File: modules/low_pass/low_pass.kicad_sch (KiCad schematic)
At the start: 35 parts, among them U1 MCP6002-xSN, U2 VTL5C, U3 MCP6002-xSN, U4 MCP6002-xSN, U5 VTL5C, U6 VTL5C

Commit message: Introduced new low_pass gate.
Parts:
- removed C5, C6: 1nf, Capacitor_SMD:C_0402_1005Metric, symbol Device:C
- removed C7: 0.1uf, Capacitor_SMD:C_0402_1005Metric, symbol Device:C
- removed D1: LED, LED_SMD:LED_0603_1608Metric, symbol Device:LED
- removed R1, R2: 100k, Resistor_SMD:R_0402_1005Metric, symbol Device:R
- removed U1, U3, U4: MCP6002-xSN, Package_SO:SOIC-8-1EP_3.9x4.9mm_P1.27mm_EP2.29x3mm, symbol Amplifier_Operational:MCP6002-xSN
- removed U2, U5, U6: VTL5C, BreadModular_MISC:VTL5C, symbol Isolator:VTL5C
- removed V3: VSIN, symbol Simulation_SPICE:VSIN
- removed V4: 0, symbol Simulation_SPICE:VDC
- added R12, R13: 10k, symbol Device:R
- added R5: 1k, symbol Device:R
- added R6: 200k, symbol Device:R
- added U1, U3, U4: VTL5C, OptoDevice:PerkinElmer_VTL5C, symbol Isolator:VTL5C
- added U2, U5: MCP6002-xSN, symbol Amplifier_Operational:MCP6002-xSN
- added V3: 3.3, symbol Simulation_SPICE:VDC
- added V4: VSIN, symbol Simulation_SPICE:VSIN
- C1: footprint Capacitor_SMD:C_0402_1005Metric -> (none)
- C2, C3: value 0.1uf -> 10nf; footprint Capacitor_SMD:C_0402_1005Metric -> (none)
- C4: value 1nf -> 0.1uf; footprint Capacitor_SMD:C_0402_1005Metric -> (none)
- GND1: footprint Connector_PinHeader_2.54mm:PinHeader_1x05_P2.54mm_Vertical -> BreadModular_MISC:Power_Connector
- R1: renamed from R5; footprint Resistor_SMD:R_0402_1005Metric -> (none)
- R10: value 100k -> 10k; footprint Resistor_SMD:R_0402_1005Metric -> (none)
- R11: value 330 -> 1M; footprint Resistor_SMD:R_0805_2012Metric -> (none)
- R2: renamed from R6; footprint Resistor_SMD:R_0402_1005Metric -> (none)
- R3: value 100k -> 560; footprint Resistor_SMD:R_0402_1005Metric -> (none)
- R4: footprint Resistor_SMD:R_0402_1005Metric -> (none)
- R7: value 100k -> 200k; footprint Resistor_SMD:R_0402_1005Metric -> (none)
- R8: value 330 -> 560; footprint Resistor_SMD:R_0805_2012Metric -> (none)
- R9: value 1k -> 1M; footprint Resistor_SMD:R_0402_1005Metric -> (none)
- RV1: footprint BreadModular_Pots:Potentiometer_RV09 -> (none); Comment CV GAIN -> CUT OFF
- RV2: footprint BreadModular_Pots:Potentiometer_RV09 -> (none); Comment CUTOFF_FREQ -> CUT_OFF_CURVE
- V1: value 5 -> 3.3
- V_SUPPLY1: renamed from 5V1; footprint Connector_PinHeader_2.54mm:PinHeader_1x05_P2.54mm_Vertical -> BreadModular_MISC:Power_Connector
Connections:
- net AUDIO_IN: now also U1.4; no longer INPUT1.1 (Pin_1)
- net AUDIO_OUT: now also R5.2; no longer R9.2
- net GND: now also C4.2, INPUT1.5 (Pin_5), R11.1, R9.1, RV2.2, U1.1 (-), U2.4 (V-), U3.1 (-), U5.4 (V-), V3.2, V4.2; no longer C2.2, C3.2, R11.2
- net at R4.2: now also R3.2, RV1.2, U4.4
- net at R3.1: now also U1.2 (+), U3.2 (+)
- net at R4.1: now also R6.2
- net at RV2.1: now also R8.1
- net at RV2.3: no longer R8.1
- net at R7.1: now also RV1.3, U4.3, U5.6 (-), U5.7
- net V_SUPPLY: now reaches C4.1
- net V_SUPPLY: now also C1.1, R1.1, V1.1, V_SUPPLY1.1 (Pin_1), V_SUPPLY1.2 (Pin_2), V_SUPPLY1.3 (Pin_3), V_SUPPLY1.4 (Pin_4), V_SUPPLY1.5 (Pin_5), R12.1, U2.8 (V+), U5.8 (V+)
- net at R10.2: now also V3.1
- net at R7.2: now also R6.1
- net at R8.2: now also U4.1 (-)
- net at INPUT1.4 (Pin_4): now also R13.2
- net +2.5V renamed V_MID
- net V_MID: now also C2.2, C3.2, R13.1
- removed net +5V: C1.1, C2.1, C3.1, R1.1, V1.1, V_SUPPLY1.1 (Pin_1), V_SUPPLY1.2 (Pin_2), V_SUPPLY1.3 (Pin_3), V_SUPPLY1.4 (Pin_4), V_SUPPLY1.5 (Pin_5)
- net CUTOFF_CV_IN: no longer names the net of INPUT1.3 (Pin_3)
- net CUTOFF_CV_IN: now also R12.2
- net MOD_CV_IN renamed CUT_OFF_CV
- net CUT_OFF_CV: now also R10.1, R9.2, U5.3 (+); no longer RV1.2
- removed net PROCESSED_MOD_CV: R10.1, R3.2, RV2.2
- new net: C2.1, U1.3, U2.3 (+)
- new net: U4.2 (+), U5.1, U5.2 (-)
- new net: C3.1, U2.5 (+), U3.3
- new net: U2.1, U2.2 (-), U3.4
- new net: R5.1, U2.6 (-), U2.7
- new net GATE_CV: INPUT1.1 (Pin_1), R11.2, U5.5 (+), V4.1
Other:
- note added: "## 1. Core Filter This is a 2nd stage RC low pass filter with Vactrols controlling the resistors."
- note added: "## 2. Gate CV This is the CV that drives filter resistors. Since those are Vactrols, 0-VMax CV both does filter cut off modulation and act as a VCA. Here RV1, put a cap to where vactrol can drive. So, technically it's the cutt-off point controlled by a pot. pos=0.0 => low frequency pos=1.0 => high frequency"
- note added: "## 3. Cut Off CV This is another set of CV modulation, but it's changing the Cut Off position. (Just like rotating the RV1) Now RV2 act as changing the curve of CV. * pos=0.0 => Exponential Curve * pos=1.0 => Linear Curve"
- note removed: "## 1. PROCESS MOD CV Here we get some CV for modulation of the cuff of frquency. We assume it will be centered around 2.5V. Basically, this is summing amp with 2.5 as the virtual GND. It will wiggle around 2.5V. If no CV input, output is 2.5V."
- note removed: "## 2. Sallen Key Filter This is a very basic Sallen Key Filter and R1 and R2 is replaced with VTL5Cs."
- note removed: "## 3. Cut Of freqeuncy CutOff frequency of Sallen Key Filter is depend on the R1 and R2. They need to be equal too. Here we set R1 based on VTL5C. So it behaves based on the Voltage input for the LED. We set 2.5V as the base potentiometer is used to change the frequency. pos=0.0 is the minimum frequency. pos=1.0 is maximum freq."
- note removed: "## 4 CutOFF freq CV This is about adding a parallel resistor to the potentiometer resistance. So, we can set the maximum it can have. (Basically overriding the pot value) Yes, we use VTL5C. So: CV=0v => Maxiumum Resistance (So, 1M pot has full control) CV=5v => Min Resistance (Pot has no control and we are in the upper cutoff freq.)"
- note removed: "## 5. Driving LED for Modulation CV It's quite useful to see this. We can directly connect the LED to the processed CV out. But it leaks audio to the ground when a square wave is provided. So, we need to smooth out the input before sending to the LED. So, we use a RC filter and a opamp. We can use a transistor instead, but it tend to leak a bit. That's why we use am opamp."
- moved on the sheet: GND1, INPUT1, OUTPUT1, R1, R2, V1, V_SUPPLY1

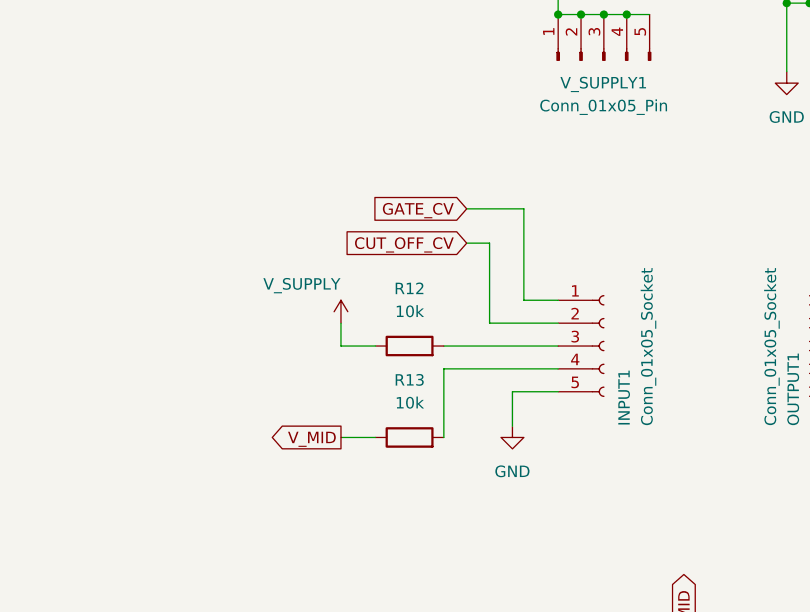
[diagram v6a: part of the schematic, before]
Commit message: Finalized the schematic of low_pass
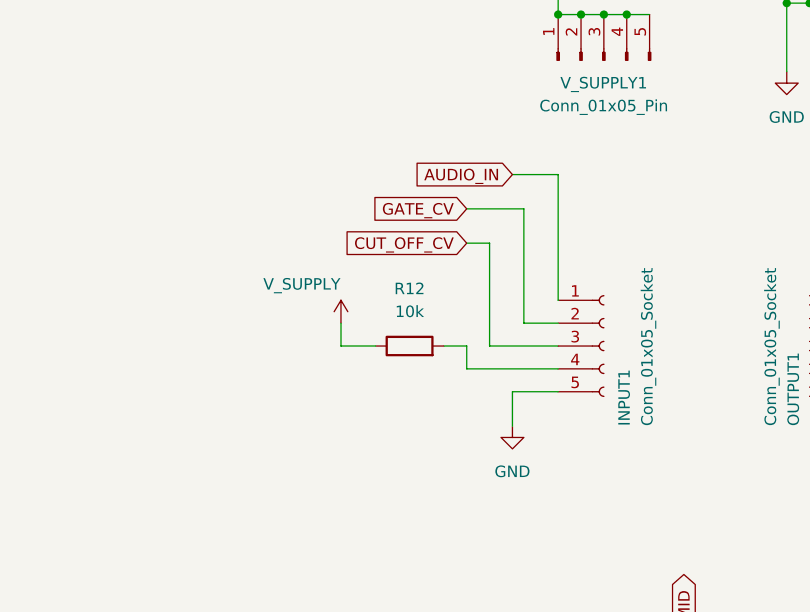
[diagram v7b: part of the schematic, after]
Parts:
- removed R13: 10k, symbol Device:R
- C1, C2, C3, C4: footprint (none) -> Capacitor_SMD:C_0402_1005Metric
- R1, R10, R11, R12, R2, R3, R4, R5, R6, R7, R8, R9: footprint (none) -> Resistor_SMD:R_0402_1005Metric
- RV1, RV2: footprint (none) -> BreadModular_Pots:Potentiometer_RV09
- U1, U3, U4: footprint OptoDevice:PerkinElmer_VTL5C -> BreadModular_MISC:VTL5C
- U2, U5: footprint (none) -> Package_SO:SOIC-8-1EP_3.9x4.9mm_P1.27mm_EP2.29x3mm
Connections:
- net AUDIO_IN: now also INPUT1.1 (Pin_1)
- net CUT_OFF_CV: now also INPUT1.3 (Pin_3); no longer INPUT1.2 (Pin_2)
- net GATE_CV: now also INPUT1.2 (Pin_2); no longer INPUT1.1 (Pin_1)
- net at INPUT1.4 (Pin_4): now also R12.2
